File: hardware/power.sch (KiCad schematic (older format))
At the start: 10 parts, among them J2 V_MEAS, J3 A_MEAS, J4 5V_IN, J5 V_MEAS, J6 A_MEAS, J7 5V_IN

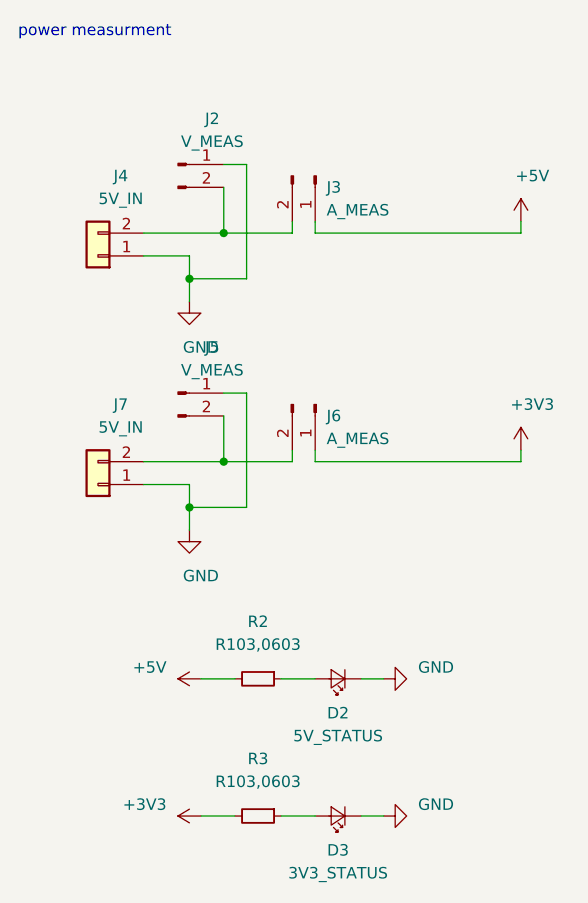
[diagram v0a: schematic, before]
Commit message: update power schematic,
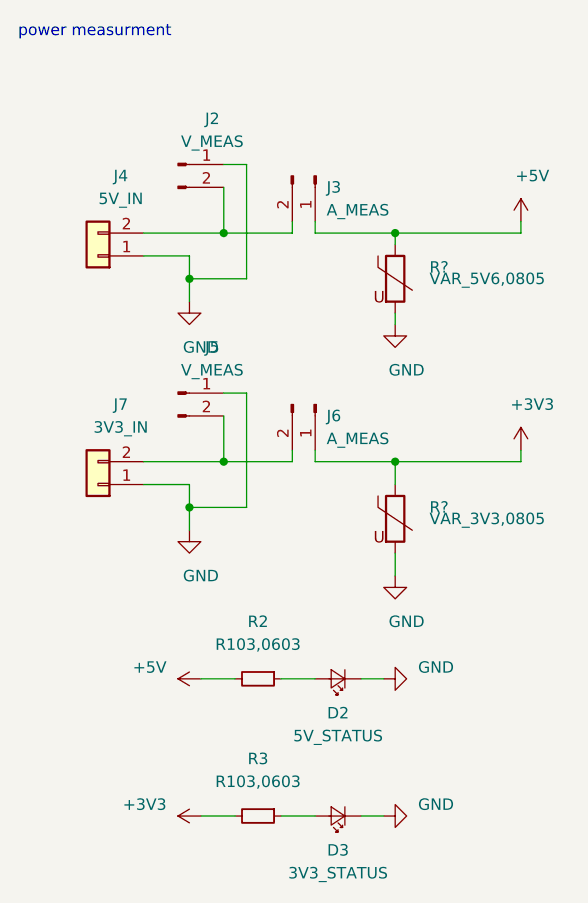
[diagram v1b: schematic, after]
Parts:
- added R?: VAR_5V6,0805, footprint-lib:VAR_0805, symbol taobao-varistor:VAR_5V6,0805
- added R?: VAR_3V3,0805, footprint-lib:VAR_0805, symbol taobao-varistor:VAR_3V3,0805
- J7: value 5V_IN -> 3V3_IN
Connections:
- net +3V3: now also R?.1
- net +5V: now also R?.1
- net GND: now also R?.2, R?.2
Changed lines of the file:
@@
 AR Path="/5CDAB997/5CDC08AC" Ref="J3"  Part="1"
 AR Path="/5CE8F13F/5CDC08AC" Ref="J?"  Part="1"
-F 0 "J?" V 2050 1500 50  0000 L CNN
+F 0 "J3" V 2050 1500 50  0000 L CNN
 F 1 "A_MEAS" V 2150 1500 50  0000 L CNN
 F 2 "" H 2000 1450 50  0001 C CNN
@@
 AR Path="/5CDAB997/5CDC1537" Ref="J4"  Part="1"
 AR Path="/5CE8F13F/5CDC1537" Ref="J?"  Part="1"
-F 0 "J?" H 950 1450 50  0000 C CNN
+F 0 "J4" H 950 1450 50  0000 C CNN
 F 1 "5V_IN" H 950 1550 50  0000 C CNN
 F 2 "" H 1050 1800 50  0001 C CNN
@@
 AR Path="/5CDAB997/5CDC1A75" Ref="#PWR0113"  Part="1"
 AR Path="/5CE8F13F/5CDC1A75" Ref="#PWR?"  Part="1"
-F 0 "#PWR?" H 1450 1750 50  0001 C CNN
+F 0 "#PWR0113" H 1450 1750 50  0001 C CNN
 F 1 "GND" H 1500 1800 50  0000 C CNN
 F 2 "" H 1450 2000 50  0001 C CNN
@@
 AR Path="/5CDAB997/5CDC22C8" Ref="J2"  Part="1"
 AR Path="/5CE8F13F/5CDC22C8" Ref="J?"  Part="1"
-F 0 "J?" H 1550 1600 50  0000 C CNN
+F 0 "J2" H 1550 1600 50  0000 C CNN
 F 1 "V_MEAS" H 1550 1500 50  0000 C CNN
 F 2 "" H 1400 1400 50  0001 C CNN
@@
 AR Path="/5CDAB997/5CDC5556" Ref="#PWR0114"  Part="1"
 AR Path="/5CE8F13F/5CDC5556" Ref="#PWR?"  Part="1"
-F 0 "#PWR?" H 2900 1500 50  0001 C CNN
+F 0 "#PWR0114" H 2900 1500 50  0001 C CNN
 F 1 "+5V" H 2950 1850 50  0000 C CNN
 F 2 "" H 2900 1650 50  0001 C CNN
@@
 	2900 1650 2900 1700
 Wire Wire Line
-	2900 1700 2000 1700
+	2900 1700 2350 1700
 Wire Wire Line
 	2000 1700 2000 1650
@@
 AR Path="/5CDAB997/5CDC6A22" Ref="J6"  Part="1"
 AR Path="/5CE8F13F/5CDC6A22" Ref="J?"  Part="1"
-F 0 "J?" V 2050 2500 50  0000 L CNN
+F 0 "J6" V 2050 2500 50  0000 L CNN
 F 1 "A_MEAS" V 2150 2500 50  0000 L CNN
 F 2 "" H 2000 2450 50  0001 C CNN
@@
 AR Path="/5CDAB997/5CDC6A2C" Ref="J7"  Part="1"
 AR Path="/5CE8F13F/5CDC6A2C" Ref="J?"  Part="1"
-F 0 "J?" H 950 2450 50  0000 C CNN
-F 1 "5V_IN" H 950 2550 50  0000 C CNN
+F 0 "J7" H 950 2450 50  0000 C CNN
+F 1 "3V3_IN" H 950 2550 50  0000 C CNN
 F 2 "" H 1050 2800 50  0001 C CNN
 F 3 "~" H 1050 2800 50  0001 C CNN
@@
 AR Path="/5CDAB997/5CDC6A36" Ref="#PWR0115"  Part="1"
 AR Path="/5CE8F13F/5CDC6A36" Ref="#PWR?"  Part="1"
-F 0 "#PWR?" H 1450 2750 50  0001 C CNN
+F 0 "#PWR0115" H 1450 2750 50  0001 C CNN
 F 1 "GND" H 1500 2800 50  0000 C CNN
 F 2 "" H 1450 3000 50  0001 C CNN
@@
 AR Path="/5CDAB997/5CDC6A42" Ref="J5"  Part="1"
 AR Path="/5CE8F13F/5CDC6A42" Ref="J?"  Part="1"
-F 0 "J?" H 1550 2600 50  0000 C CNN
+F 0 "J5" H 1550 2600 50  0000 C CNN
 F 1 "V_MEAS" H 1550 2500 50  0000 C CNN
 F 2 "" H 1400 2400 50  0001 C CNN
@@
 	2900 2650 2900 2700
 Wire Wire Line
-	2900 2700 2000 2700
+	2900 2700 2350 2700
 Wire Wire Line
 	2000 2700 2000 2650
@@
 AR Path="/5CDAB997/5CDC8B9F" Ref="#PWR0116"  Part="1"
 AR Path="/5CE8F13F/5CDC8B9F" Ref="#PWR?"  Part="1"
-F 0 "#PWR?" H 2900 2500 50  0001 C CNN
+F 0 "#PWR0116" H 2900 2500 50  0001 C CNN
 F 1 "+3V3" H 2950 2850 50  0000 C CNN
 F 2 "" H 2900 2650 50  0001 C CNN
@@
 AR Path="/5CDAB997/5CDD6EE1" Ref="#PWR0117"  Part="1"
 AR Path="/5CE8F13F/5CDD6EE1" Ref="#PWR?"  Part="1"
-F 0 "#PWR?" H 1500 3500 50  0001 C CNN
+F 0 "#PWR0117" H 1500 3500 50  0001 C CNN
 F 1 "+5V" V 1550 3800 50  0000 L CNN
 F 2 "" H 1500 3650 50  0001 C CNN
@@
 AR Path="/5CDAB997/5CDD7398" Ref="R2"  Part="1"
 AR Path="/5CE8F13F/5CDD7398" Ref="R?"  Part="1"
-F 0 "R?" V 1500 3650 50  0000 C CNN
+F 0 "R2" V 1500 3650 50  0000 C CNN
 F 1 "R103,0603" V 1600 3650 50  0000 C CNN
 F 2 "Resistor_SMD:R_0603_1608Metric_Pad1.05x0.95mm_HandSolder" H 1750 3650 50  0001 C CNN
@@
 AR Path="/5CDAB997/5CDD808A" Ref="D2"  Part="1"
 AR Path="/5CE8F13F/5CDD808A" Ref="D?"  Part="1"
-F 0 "D?" H 2100 3800 50  0000 C CNN
+F 0 "D2" H 2100 3800 50  0000 C CNN
 F 1 "5V_STATUS" H 2100 3900 50  0000 C CNN
 F 2 "LED_SMD:LED_0603_1608Metric_Pad1.05x0.95mm_HandSolder" V 2100 3650 50  0001 C CNN
@@
 AR Path="/5CDAB997/5CDD83E9" Ref="#PWR0118"  Part="1"
 AR Path="/5CE8F13F/5CDD83E9" Ref="#PWR?"  Part="1"
-F 0 "#PWR?" H 2300 3400 50  0001 C CNN
+F 0 "#PWR0118" H 2300 3400 50  0001 C CNN
 F 1 "GND" V 2350 3500 50  0000 R CNN
 F 2 "" H 2300 3650 50  0001 C CNN
@@
 AR Path="/5CDAB997/5CDDC8A9" Ref="R3"  Part="1"
 AR Path="/5CE8F13F/5CDDC8A9" Ref="R?"  Part="1"
-F 0 "R?" V 1500 4250 50  0000 C CNN
+F 0 "R3" V 1500 4250 50  0000 C CNN
 F 1 "R103,0603" V 1600 4250 50  0000 C CNN
 F 2 "Resistor_SMD:R_0603_1608Metric_Pad1.05x0.95mm_HandSolder" H 1750 4250 50  0001 C CNN
@@
 AR Path="/5CDAB997/5CDDC8B3" Ref="D3"  Part="1"
 AR Path="/5CE8F13F/5CDDC8B3" Ref="D?"  Part="1"
-F 0 "D?" H 2100 4400 50  0000 C CNN
+F 0 "D3" H 2100 4400 50  0000 C CNN
 F 1 "3V3_STATUS" H 2100 4500 50  0000 C CNN
 F 2 "LED_SMD:LED_0603_1608Metric_Pad1.05x0.95mm_HandSolder" V 2100 4250 50  0001 C CNN
@@
 AR Path="/5CDAB997/5CDDC8BD" Ref="#PWR0119"  Part="1"
 AR Path="/5CE8F13F/5CDDC8BD" Ref="#PWR?"  Part="1"
-F 0 "#PWR?" H 2300 4000 50  0001 C CNN
+F 0 "#PWR0119" H 2300 4000 50  0001 C CNN
 F 1 "GND" V 2350 4100 50  0000 R CNN
 F 2 "" H 2300 4250 50  0001 C CNN
@@
 AR Path="/5CDAB997/5CDDDD9C" Ref="#PWR0120"  Part="1"
 AR Path="/5CE8F13F/5CDDDD9C" Ref="#PWR?"  Part="1"
-F 0 "#PWR?" H 1500 4100 50  0001 C CNN
+F 0 "#PWR0120" H 1500 4100 50  0001 C CNN
 F 1 "+3V3" V 1550 4400 50  0000 L CNN
 F 2 "" H 1500 4250 50  0001 C CNN
@@
 	0    -1   -1   0
 $EndComp
+$Comp
+L taobao-varistor:VAR_5V6,0805 R?
+U 1 1 5CE50EF8
+P 2350 1900
+F 0 "R?" H 2500 1950 50  0000 L CNN
+F 1 "VAR_5V6,0805" H 2500 1900 50  0000 L CNN
+F 2 "footprint-lib:VAR_0805" H 2350 1900 50  0001 C CNN
+F 3 "~" H 2350 1900 50  0001 C CNN
+	1    2350 1900
+	1    0    0    -1
+$EndComp
+Wire Wire Line
+	2350 1750 2350 1700
+Connection ~ 2350 1700
+Wire Wire Line
+	2350 1700 2000 1700
+$Comp
+L power:GND #PWR?
+U 1 1 5CE517F1
+P 2350 2100
+AR Path="/5CDAB997/5CE517F1" Ref="#PWR?"  Part="1"
+AR Path="/5CE8F13F/5CE517F1" Ref="#PWR?"  Part="1"
+F 0 "#PWR?" H 2350 1850 50  0001 C CNN
+F 1 "GND" H 2400 1900 50  0000 C CNN
+F 2 "" H 2350 2100 50  0001 C CNN
+F 3 "" H 2350 2100 50  0001 C CNN
+	1    2350 2100
+	1    0    0    -1
+$EndComp
+Wire Wire Line
+	2350 2050 2350 2100
+$Comp
+L taobao-varistor:VAR_3V3,0805 R?
+U 1 1 5CE538D7
+P 2350 2950
+F 0 "R?" H 2500 3000 50  0000 L CNN
+F 1 "VAR_3V3,0805" H 2500 2950 50  0000 L CNN
+F 2 "footprint-lib:VAR_0805" H 2350 2950 50  0001 C CNN
+F 3 "~" H 2350 2950 50  0001 C CNN
+	1    2350 2950
+	1    0    0    -1
+$EndComp
+Wire Wire Line
+	2350 2800 2350 2700
+Connection ~ 2350 2700
+Wire Wire Line
+	2350 2700 2000 2700
+$Comp
+L power:GND #PWR?
+U 1 1 5CE5450B
+P 2350 3200
+F 0 "#PWR?" H 2350 2950 50  0001 C CNN
+F 1 "GND" H 2400 3000 50  0000 C CNN
+F 2 "" H 2350 3200 50  0001 C CNN
+F 3 "" H 2350 3200 50  0001 C CNN
+	1    2350 3200
+	1    0    0    -1
+$EndComp
+Wire Wire Line
+	2350 3200 2350 3100
 $EndSCHEMATC

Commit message: update,
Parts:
- D2, D3: footprint LED_SMD:LED_0603_1608Metric_Pad1.05x0.95mm_HandSolder -> footprint-lib:LED_0603_1608Metric
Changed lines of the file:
@@
 $Descr A4 11693 8268
 encoding utf-8
-Sheet 12 21
+Sheet 11 21
 Title ""
 Date ""
@@
 F 0 "D2" H 2100 3800 50  0000 C CNN
 F 1 "5V_STATUS" H 2100 3900 50  0000 C CNN
-F 2 "LED_SMD:LED_0603_1608Metric_Pad1.05x0.95mm_HandSolder" V 2100 3650 50  0001 C CNN
+F 2 "footprint-lib:LED_0603_1608Metric" V 2100 3650 50  0001 C CNN
 F 3 "" V 2100 3650 50  0001 C CNN
 	1    2100 3650
@@
 F 0 "D3" H 2100 4400 50  0000 C CNN
 F 1 "3V3_STATUS" H 2100 4500 50  0000 C CNN
-F 2 "LED_SMD:LED_0603_1608Metric_Pad1.05x0.95mm_HandSolder" V 2100 4250 50  0001 C CNN
+F 2 "footprint-lib:LED_0603_1608Metric" V 2100 4250 50  0001 C CNN
 F 3 "" V 2100 4250 50  0001 C CNN
 	1    2100 4250

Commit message: update,
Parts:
- gave numbers to parts that had none: 2
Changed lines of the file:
@@
 $EndComp
 $Comp
-L taobao-varistor:VAR_5V6,0805 R?
+L taobao-varistor:VAR_5V6,0805 R20
 U 1 1 5CE50EF8
 P 2350 1900
-F 0 "R?" H 2500 1950 50  0000 L CNN
+F 0 "R20" H 2500 1950 50  0000 L CNN
 F 1 "VAR_5V6,0805" H 2500 1900 50  0000 L CNN
 F 2 "footprint-lib:VAR_0805" H 2350 1900 50  0001 C CNN
@@
 	2350 1700 2000 1700
 $Comp
-L power:GND #PWR?
+L power:GND #PWR0224
 U 1 1 5CE517F1
 P 2350 2100
-AR Path="/5CDAB997/5CE517F1" Ref="#PWR?"  Part="1"
+AR Path="/5CDAB997/5CE517F1" Ref="#PWR0224"  Part="1"
 AR Path="/5CE8F13F/5CE517F1" Ref="#PWR?"  Part="1"
-F 0 "#PWR?" H 2350 1850 50  0001 C CNN
+F 0 "#PWR0224" H 2350 1850 50  0001 C CNN
 F 1 "GND" H 2400 1900 50  0000 C CNN
 F 2 "" H 2350 2100 50  0001 C CNN
@@
 	2350 2050 2350 2100
 $Comp
-L taobao-varistor:VAR_3V3,0805 R?
+L taobao-varistor:VAR_3V3,0805 R21
 U 1 1 5CE538D7
 P 2350 2950
-F 0 "R?" H 2500 3000 50  0000 L CNN
+F 0 "R21" H 2500 3000 50  0000 L CNN
 F 1 "VAR_3V3,0805" H 2500 2950 50  0000 L CNN
 F 2 "footprint-lib:VAR_0805" H 2350 2950 50  0001 C CNN
@@
 	2350 2700 2000 2700
 $Comp
-L power:GND #PWR?
+L power:GND #PWR0225
 U 1 1 5CE5450B
 P 2350 3200
-F 0 "#PWR?" H 2350 2950 50  0001 C CNN
+F 0 "#PWR0225" H 2350 2950 50  0001 C CNN
 F 1 "GND" H 2400 3000 50  0000 C CNN
 F 2 "" H 2350 3200 50  0001 C CNN
